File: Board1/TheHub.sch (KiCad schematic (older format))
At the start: 42 parts, among them J11 RFD900, J12 I2C_1 Test Point, J13 I2C_2 Test Point, J15 GPIO Test, J16 I2C_3 Test Point, J17 12V OUT, J18 7.4V IN, J23 NucleoRight, J5 NucleoLeft, J8 12V MAIN POWER, U10 ADXL377, U11 BNO055, U12 MPL115A2, U13 GPS, U6 TL1963, U7 LM340MP-5.0, U8 MCP9808

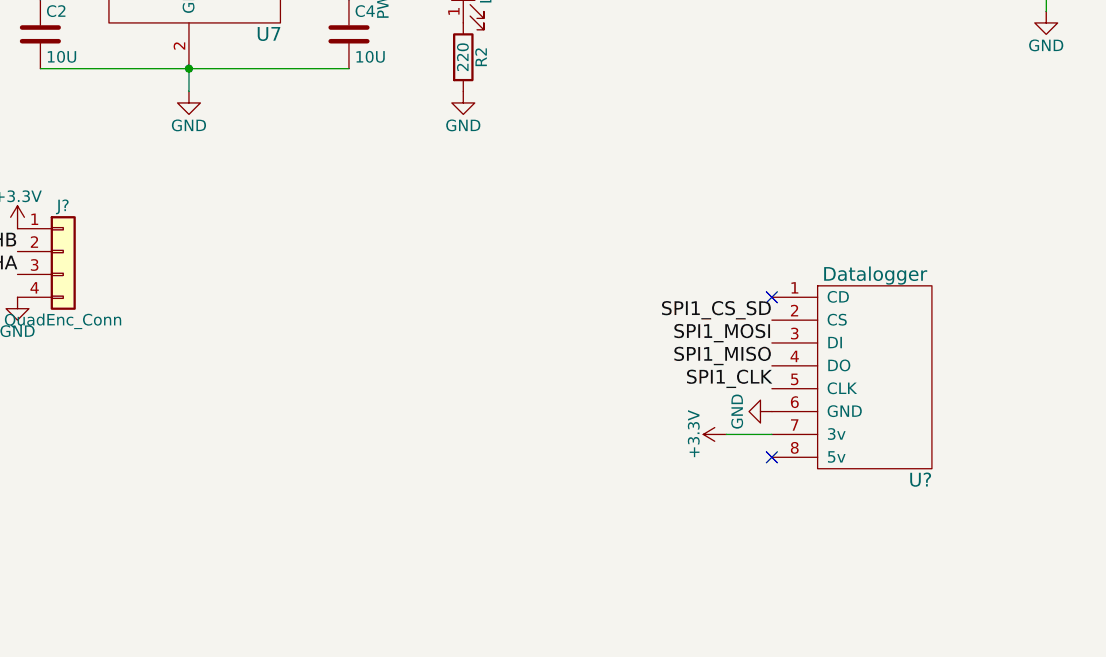
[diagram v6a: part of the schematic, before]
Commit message: Add DS3231 to schematic lib, integrate DS3231 into schematic
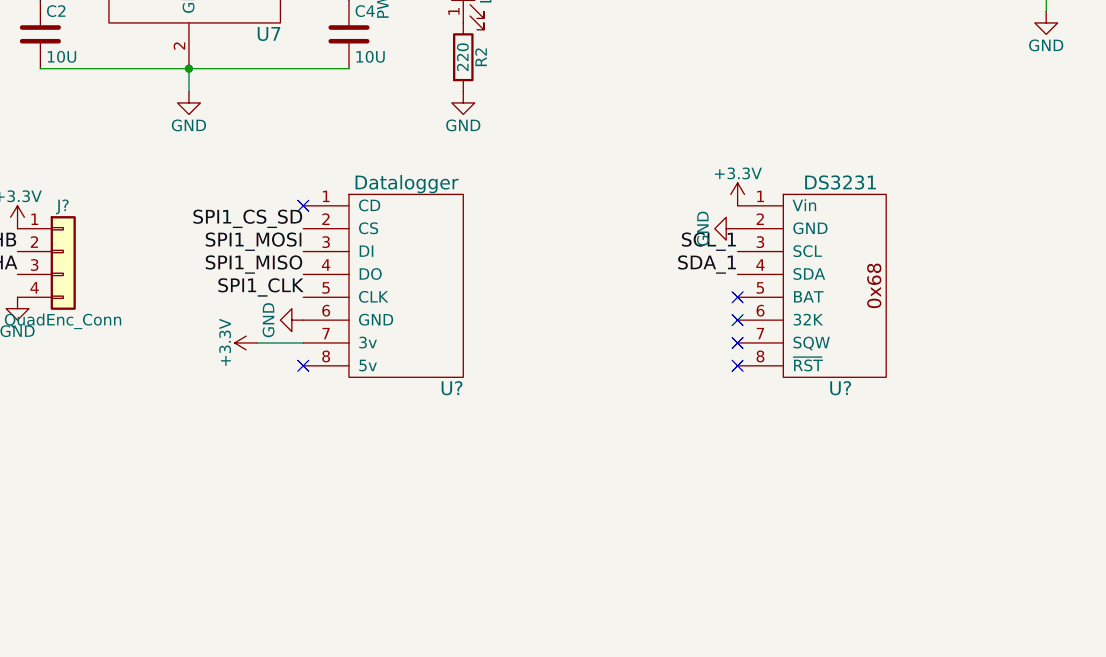
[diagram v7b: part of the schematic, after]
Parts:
- added U?: DS3231, symbol DS3231
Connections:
- net +3V3: now also U?.1 (Vin)
- net GND: now also U?.2 (GND)
- net PB6: now also U?.3 (SCL)
- net PB7: now also U?.4 (SDA)
- no-connect marks 39 -> 43
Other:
- moved on the sheet: U?
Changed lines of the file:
@@
 L Datalogger U?
 U 1 1 5A670F4A
-P 12650 5500
-F 0 "U?" H 13100 5600 60  0000 C CNN
-F 1 "Datalogger" H 12900 6500 60  0000 C CNN
-F 2 "" H 12650 5500 60  0001 C CNN
-F 3 "" H 12650 5500 60  0001 C CNN
-	1    12650 5500
+P 10600 5100
+F 0 "U?" H 11050 5200 60  0000 C CNN
+F 1 "Datalogger" H 10850 6100 60  0000 C CNN
+F 2 "" H 10600 5100 60  0001 C CNN
+F 3 "" H 10600 5100 60  0001 C CNN
+	1    10600 5100
 	1    0    0    -1
 $EndComp
-Text Label 12450 4700 2    60   ~ 0
+Text Label 10400 4300 2    60   ~ 0
 SPI1_CS_SD
-Text Label 12450 4800 2    60   ~ 0
+Text Label 10400 4400 2    60   ~ 0
 SPI1_MOSI
-Text Label 12450 4900 2    60   ~ 0
+Text Label 10400 4500 2    60   ~ 0
 SPI1_MISO
 Wire Wire Line
@@
 Text Label 5050 2450 2    60   ~ 0
 SPI1_CLK
-Text Label 12450 5000 2    60   ~ 0
+Text Label 10400 4600 2    60   ~ 0
 SPI1_CLK
 $Comp
 L GND #PWR?
 U 1 1 5A676B6D
-P 12450 5100
-F 0 "#PWR?" H 12450 4850 50  0001 C CNN
-F 1 "GND" H 12450 4950 50  0000 C CNN
-F 2 "" H 12450 5100 50  0001 C CNN
-F 3 "" H 12450 5100 50  0001 C CNN
-	1    12450 5100
+P 10400 4700
+F 0 "#PWR?" H 10400 4450 50  0001 C CNN
+F 1 "GND" H 10400 4550 50  0000 C CNN
+F 2 "" H 10400 4700 50  0001 C CNN
+F 3 "" H 10400 4700 50  0001 C CNN
+	1    10400 4700
 	0    1    1    0
 $EndComp
@@
 L +3.3V #PWR?
 U 1 1 5A676BD5
-P 12250 5200
-F 0 "#PWR?" H 12250 5050 50  0001 C CNN
-F 1 "+3.3V" H 12250 5340 50  0000 C CNN
-F 2 "" H 12250 5200 50  0001 C CNN
-F 3 "" H 12250 5200 50  0001 C CNN
-	1    12250 5200
+P 10200 4800
+F 0 "#PWR?" H 10200 4650 50  0001 C CNN
+F 1 "+3.3V" H 10200 4940 50  0000 C CNN
+F 2 "" H 10200 4800 50  0001 C CNN
+F 3 "" H 10200 4800 50  0001 C CNN
+	1    10200 4800
 	0    -1   -1   0
 $EndComp
 Wire Wire Line
-	12250 5200 12450 5200
-NoConn ~ 12450 4600
-NoConn ~ 12450 5300
+	10200 4800 10400 4800
+NoConn ~ 10400 4200
+NoConn ~ 10400 4900
+$Comp
+L DS3231 U?
+U 1 1 5A683162
+P 12700 4600
+F 0 "U?" H 12750 4200 60  0000 C CNN
+F 1 "DS3231" H 12750 5100 60  0000 C CNN
+F 2 "" H 12700 4600 60  0001 C CNN
+F 3 "" H 12700 4600 60  0001 C CNN
+	1    12700 4600
+	1    0    0    -1
+$EndComp
+$Comp
+L +3.3V #PWR?
+U 1 1 5A684124
+P 12300 4200
+F 0 "#PWR?" H 12300 4050 50  0001 C CNN
+F 1 "+3.3V" H 12300 4340 50  0000 C CNN
+F 2 "" H 12300 4200 50  0001 C CNN
+F 3 "" H 12300 4200 50  0001 C CNN
+	1    12300 4200
+	1    0    0    -1
+$EndComp
+$Comp
+L GND #PWR?
+U 1 1 5A68418E
+P 12300 4300
+F 0 "#PWR?" H 12300 4050 50  0001 C CNN
+F 1 "GND" H 12300 4150 50  0000 C CNN
+F 2 "" H 12300 4300 50  0001 C CNN
+F 3 "" H 12300 4300 50  0001 C CNN
+	1    12300 4300
+	0    1    1    0
+$EndComp
+Text Label 12300 4500 2    60   ~ 0
+SDA_1
+Text Label 12300 4400 2    60   ~ 0
+SCL_1
+NoConn ~ 12300 4600
+NoConn ~ 12300 4700
+NoConn ~ 12300 4800
+NoConn ~ 12300 4900
 $EndSCHEMATC
